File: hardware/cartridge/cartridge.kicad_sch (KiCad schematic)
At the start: 19 parts, among them U1 SN74LVC8T245PWR, U2 SN74LVC8T245PWR, U3 SN74LVC8T245PWR, U4 SN74LVC8T245PWR, U5 LCMXO2-1200HC-4TG100C, U6 MX29LV320EBTI-70G, U7 FM28V100-TG

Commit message: Fix ROM memory connections
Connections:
- net +3.3V: now also C9.1, U6.14 (WP#/ACC), U6.37 (VCC)
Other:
- moved on the sheet: C9
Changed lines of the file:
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@@
 	)
 	(junction
+		(at 129.54 60.96)
+		(diameter 0)
+		(color 0 0 0 0)
+	)
+	(junction
 		(at 351.79 227.33)
 		(diameter 0)
@@
 	(wire
 		(pts
-			(xy 107.95 60.96) (xy 125.73 60.96)
+			(xy 107.95 60.96) (xy 129.54 60.96)
 		)
 		(stroke
@@
 	(symbol
 		(lib_id "power:GND")
-		(at 133.35 60.96 90)
+		(at 137.16 60.96 90)
 		(unit 1)
 		(body_style 1)
@@
 		(fields_autoplaced yes)
 		(property "Reference" "#PWR0138"
-			(at 139.7 60.96 0)
+			(at 143.51 60.96 0)
 			(hide yes)
 			(show_name no)
@@
 		)
 		(property "Value" "GND"
-			(at 137.16 60.9599 90)
+			(at 140.97 60.9599 90)
 			(show_name no)
 			(do_not_autoplace no)
@@
 		)
 		(property "Footprint" ""
-			(at 133.35 60.96 0)
+			(at 137.16 60.96 0)
 			(hide yes)
 			(show_name no)
@@
 		)
 		(property "Datasheet" ""
-			(at 133.35 60.96 0)
+			(at 137.16 60.96 0)
 			(hide yes)
 			(show_name no)
@@
 		)
 		(property "Description" "Power symbol creates a global label with name \"GND\" , ground"
-			(at 133.35 60.96 0)
+			(at 137.16 60.96 0)
 			(hide yes)
 			(show_name no)
@@
 	)
 	(symbol
+		(lib_id "power:+3.3V")
+		(at 129.54 60.96 180)
+		(unit 1)
+		(body_style 1)
+		(exclude_from_sim no)
+		(in_bom yes)
+		(on_board yes)
+		(in_pos_files yes)
+		(dnp no)
+		(fields_autoplaced yes)
+		(property "Reference" "#PWR0292"
+			(at 129.54 57.15 0)
+			(hide yes)
+			(show_name no)
+			(do_not_autoplace no)
+			(effects
+				(font
+					(size 1.27 1.27)
+				)
+			)
+		)
+		(property "Value" "+3.3V"
+			(at 129.54 66.04 0)
+			(show_name no)
+			(do_not_autoplace no)
+			(effects
+				(font
+					(size 1.27 1.27)
+				)
+			)
+		)
+		(property "Footprint" ""
+			(at 129.54 60.96 0)
+			(hide yes)
+			(show_name no)
+			(do_not_autoplace no)
+			(effects
+				(font
+					(size 1.27 1.27)
+				)
+			)
+		)
+		(property "Datasheet" ""
+			(at 129.54 60.96 0)
+			(hide yes)
+			(show_name no)
+			(do_not_autoplace no)
+			(effects
+				(font
+					(size 1.27 1.27)
+				)
+			)
+		)
+		(property "Description" "Power symbol creates a global label with name \"+3.3V\""
+			(at 129.54 60.96 0)
+			(hide yes)
+			(show_name no)
+			(do_not_autoplace no)
+			(effects
+				(font
+					(size 1.27 1.27)
+				)
+			)
+		)
+		(pin "1"
+		)
+		(instances
+			(project "cartridge"
+				(path "/2780facd-cffd-485a-aed1-c460c817db24"
+					(reference "#PWR0292")
+					(unit 1)
+				)
+			)
+		)
+	)
+	(symbol
 		(lib_id "power:GND")
 		(at 242.57 182.88 90)
@@
 	)
 	(symbol
+		(lib_id "power:+3.3V")
+		(at 57.15 66.04 90)
+		(unit 1)
+		(body_style 1)
+		(exclude_from_sim no)
+		(in_bom yes)
+		(on_board yes)
+		(in_pos_files yes)
+		(dnp no)
+		(fields_autoplaced yes)
+		(property "Reference" "#PWR0293"
+			(at 60.96 66.04 0)
+			(hide yes)
+			(show_name no)
+			(do_not_autoplace no)
+			(effects
+				(font
+					(size 1.27 1.27)
+				)
+			)
+		)
+		(property "Value" "+3.3V"
+			(at 53.34 66.0399 90)
+			(show_name no)
+			(do_not_autoplace no)
+			(effects
+				(font
+					(size 1.27 1.27)
+				)
+				(justify left)
+			)
+		)
+		(property "Footprint" ""
+			(at 57.15 66.04 0)
+			(hide yes)
+			(show_name no)
+			(do_not_autoplace no)
+			(effects
+				(font
+					(size 1.27 1.27)
+				)
+			)
+		)
+		(property "Datasheet" ""
+			(at 57.15 66.04 0)
+			(hide yes)
+			(show_name no)
+			(do_not_autoplace no)
+			(effects
+				(font
+					(size 1.27 1.27)
+				)
+			)
+		)
+		(property "Description" "Power symbol creates a global label with name \"+3.3V\""
+			(at 57.15 66.04 0)
+			(hide yes)
+			(show_name no)
+			(do_not_autoplace no)
+			(effects
+				(font
+					(size 1.27 1.27)
+				)
+			)
+		)
+		(pin "1"
+		)
+		(instances
+			(project "cartridge"
+				(path "/2780facd-cffd-485a-aed1-c460c817db24"
+					(reference "#PWR0293")
+					(unit 1)
+				)
+			)
+		)
+	)
+	(symbol
 		(lib_id "power:VSSA")
 		(at 351.79 219.71 270)
@@
 	(symbol
 		(lib_id "Device:C")
-		(at 129.54 60.96 90)
+		(at 133.35 60.96 90)
 		(unit 1)
 		(body_style 1)
@@
 		(fields_autoplaced yes)
 		(property "Reference" "C9"
-			(at 129.54 53.34 90)
+			(at 133.35 53.34 90)
 			(show_name no)
 			(do_not_autoplace no)
@@
 		)
 		(property "Value" "100nF"
-			(at 129.54 55.88 90)
+			(at 133.35 55.88 90)
 			(show_name no)
 			(do_not_autoplace no)
@@
 		)
 		(property "Footprint" "Capacitor_SMD:C_0603_1608Metric_Pad1.08x0.95mm_HandSolder"
-			(at 133.35 59.9948 0)
+			(at 137.16 59.9948 0)
 			(hide yes)
 			(show_name no)
@@
 		)
 		(property "Datasheet" ""
-			(at 129.54 60.96 0)
+			(at 133.35 60.96 0)
 			(hide yes)
 			(show_name no)
@@
 		)
 		(property "Description" "Unpolarized capacitor"
-			(at 129.54 60.96 0)
+			(at 133.35 60.96 0)
 			(hide yes)
 			(show_name no)

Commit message: Add PCB
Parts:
- U1, U2, U3, U4: footprint PW24 -> SN74LVC8T245PWR:PW24
- U5: footprint TQFP100_LAT -> LCMXO2-1200HC-4TG100C:TQFP100_LAT
- U6: footprint TSOPI48L12X20NORMAL_MAC -> MX29LV320EBTI-70G:TSOPI48L12X20NORMAL_MAC
- U7: footprint TSOP-32 -> FM28V100-TG:TSOP-32
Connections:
- net gb_a1: now also U1.3 (A1)
- net gb_a10: no longer U1.5 (A3)
- net gb_a11: no longer U1.6 (A4)
- net gb_a12: no longer U1.7 (A5)
- net gb_a13: no longer U1.8 (A6)
- net gb_a14: no longer U1.9 (A7)
- net gb_a15: no longer U1.10 (A8)
- net gb_a2: now also U1.4 (A2)
- net gb_a3: now also U1.5 (A3)
- net gb_a4: now also U1.6 (A4)
- net gb_a5: now also U1.7 (A5)
- net gb_a6: now also U1.8 (A6)
- net gb_a7: now also U1.9 (A7)
- net gb_a8: now also U1.10 (A8); no longer U1.3 (A1)
- net gb_a9: no longer U1.4 (A2)
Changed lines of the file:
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@@
 			)
 		)
-		(property "Footprint" "PW24"
+		(property "Footprint" "SN74LVC8T245PWR:PW24"
 			(at 182.88 207.01 0)
 			(hide yes)
@@
 			)
 		)
-		(property "Footprint" "TQFP100_LAT"
+		(property "Footprint" "LCMXO2-1200HC-4TG100C:TQFP100_LAT"
 			(at 57.15 121.92 0)
 			(hide yes)
@@
 		(in_pos_files yes)
 		(dnp no)
-		(fields_autoplaced yes)
 		(property "Reference" "#PWR046"
 			(at 185.42 160.02 0)
@@
 			)
 		)
-		(property "Value" "gb_a8"
-			(at 177.8 160.0199 90)
+		(property "Value" "gb_a1"
+			(at 175.006 160.02 90)
 			(show_name no)
 			(do_not_autoplace no)
@@
 					(size 1.27 1.27)
 				)
-				(justify left)
 			)
 		)
@@
 		(in_pos_files yes)
 		(dnp no)
-		(fields_autoplaced yes)
 		(property "Reference" "#PWR067"
 			(at 185.42 165.1 0)
@@
 			)
 		)
-		(property "Value" "gb_a10"
-			(at 177.8 165.0999 90)
+		(property "Value" "gb_a3"
+			(at 174.752 165.1 90)
 			(show_name no)
 			(do_not_autoplace no)
@@
 					(size 1.27 1.27)
 				)
-				(justify left)
 			)
 		)
@@
 		(in_pos_files yes)
 		(dnp no)
-		(fields_autoplaced yes)
 		(property "Reference" "#PWR0209"
 			(at 185.42 177.8 0)
@@
 			)
 		)
-		(property "Value" "gb_a15"
-			(at 177.8 177.7999 90)
+		(property "Value" "gb_a8"
+			(at 174.752 177.546 90)
 			(show_name no)
 			(do_not_autoplace no)
@@
 					(size 1.27 1.27)
 				)
-				(justify left)
 			)
 		)
@@
 		(in_pos_files yes)
 		(dnp no)
-		(fields_autoplaced yes)
 		(property "Reference" "#PWR0208"
 			(at 185.42 175.26 0)
@@
 			)
 		)
-		(property "Value" "gb_a14"
-			(at 177.8 175.2599 90)
+		(property "Value" "gb_a7"
+			(at 174.752 175.26 90)
 			(show_name no)
 			(do_not_autoplace no)
@@
 					(size 1.27 1.27)
 				)
-				(justify left)
 			)
 		)
@@
 		(in_pos_files yes)
 		(dnp no)
-		(fields_autoplaced yes)
 		(property "Reference" "#PWR049"
 			(at 185.42 162.56 0)
@@
 			)
 		)
-		(property "Value" "gb_a9"
-			(at 177.8 162.5599 90)
+		(property "Value" "gb_a2"
+			(at 174.752 162.56 90)
 			(show_name no)
 			(do_not_autoplace no)
@@
 					(size 1.27 1.27)
 				)
-				(justify left)
 			)
 		)
@@
 			)
 		)
-		(property "Footprint" "PW24"
+		(property "Footprint" "SN74LVC8T245PWR:PW24"
 			(at 181.61 154.94 0)
 			(hide yes)
@@
 		(in_pos_files yes)
 		(dnp no)
-		(fields_autoplaced yes)
 		(property "Reference" "#PWR0206"
 			(at 185.42 170.18 0)
@@
 			)
 		)
-		(property "Value" "gb_a12"
-			(at 177.8 170.1799 90)
+		(property "Value" "gb_a5"
+			(at 174.752 170.18 90)
 			(show_name no)
 			(do_not_autoplace no)
@@
 					(size 1.27 1.27)
 				)
-				(justify left)
 			)
 		)
@@
 		(in_pos_files yes)
 		(dnp no)
-		(fields_autoplaced yes)
 		(property "Reference" "#PWR088"
 			(at 185.42 167.64 0)
@@
 			)
 		)
-		(property "Value" "gb_a11"
-			(at 177.8 167.6399 90)
+		(property "Value" "gb_a4"
+			(at 174.752 167.64 90)
 			(show_name no)
 			(do_not_autoplace no)
@@
 					(size 1.27 1.27)
 				)
-				(justify left)
 			)
 		)
@@
 			)
 		)
-		(property "Footprint" "TSOPI48L12X20NORMAL_MAC"
+		(property "Footprint" "MX29LV320EBTI-70G:TSOPI48L12X20NORMAL_MAC"
 			(at 57.15 33.02 0)
 			(hide yes)
@@
 			)
 		)
-		(property "Footprint" "PW24"
+		(property "Footprint" "SN74LVC8T245PWR:PW24"
 			(at 290.83 207.01 0)
 			(hide yes)
@@
 			)
 		)
-		(property "Footprint" "TSOP-32"
+		(property "Footprint" "FM28V100-TG:TSOP-32"
 			(at 185.42 31.75 0)
 			(hide yes)
@@
 		(in_pos_files yes)
 		(dnp no)
-		(fields_autoplaced yes)
 		(property "Reference" "#PWR0207"
 			(at 185.42 172.72 0)
@@
 			)
 		)
-		(property "Value" "gb_a13"
-			(at 177.8 172.7199 90)
+		(property "Value" "gb_a6"
+			(at 174.752 172.72 90)
 			(show_name no)
 			(do_not_autoplace no)
@@
 					(size 1.27 1.27)
 				)
-				(justify left)
 			)
 		)
@@
 			)
 		)
-		(property "Footprint" "PW24"
+		(property "Footprint" "SN74LVC8T245PWR:PW24"
 			(at 290.83 154.94 0)
 			(hide yes)

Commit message: Add RP2040, caps, 3D models
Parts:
- added C11, C12, C13, C14, C15, C16, C17, C18, C19, C20: 100nF, Capacitor_SMD:C_0603_1608Metric_Pad1.08x0.95mm_HandSolder, symbol Device:C
- added R4: 10K, Resistor_SMD:R_0603_1608Metric_Pad0.98x0.95mm_HandSolder, symbol Device:R
- added U8: RP2040-Zero, RP2040-Zero:RP2040-Zero, symbol RP2040-Zero:RP2040-Zero
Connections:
- net +3.3V: now also C11.1, C12.1, C13.1, C14.1, C15.1, C16.1, C17.1, C18.1, C19.1, C20.1, U8.3v3
- net GND: now also C11.2, C12.2, C13.2, C14.2, C15.2, C16.2, C17.2, C18.2, C19.2, C20.2, R4.1, U8.GND
- net data_dir: now also R4.2
- new net +5V (USB): U8.5v

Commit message: Add spi_bringup (draft)
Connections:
- net SPI_MOSI: now reaches U5.96 (PT10B)
- net SPI_MOSI: now also U8.3
- net SPI_CS_N: now reaches U5.97 (PT10A)
- net SPI_CS_N: now also U8.1
- net SPI_SCK: now reaches U5.98 (PT9B)
- net SPI_SCK: now also U8.2
- net SPI_MISO: now reaches U5.99 (PT9A)
- net SPI_MISO: now also U8.0
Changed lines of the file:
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@@
 		)
+	)
+	(label "SPI_MISO"
+		(at 304.8 30.48 0)
+		(effects (font (size 1.27 1.27)) (justify left bottom))
+	)
+	(label "SPI_CS_N"
+		(at 304.8 33.02 0)
+		(effects (font (size 1.27 1.27)) (justify left bottom))
+	)
+	(label "SPI_SCK"
+		(at 304.8 35.56 0)
+		(effects (font (size 1.27 1.27)) (justify left bottom))
+	)
+	(label "SPI_MOSI"
+		(at 304.8 38.1 0)
+		(effects (font (size 1.27 1.27)) (justify left bottom))
+	)
+	(label "SPI_MISO"
+		(at 128.27 124.46 0)
+		(effects (font (size 1.27 1.27)) (justify left bottom))
+	)
+	(label "SPI_CS_N"
+		(at 128.27 129.54 0)
+		(effects (font (size 1.27 1.27)) (justify left bottom))
+	)
+	(label "SPI_SCK"
+		(at 128.27 127 0)
+		(effects (font (size 1.27 1.27)) (justify left bottom))
+	)
+	(label "SPI_MOSI"
+		(at 128.27 132.08 0)
+		(effects (font (size 1.27 1.27)) (justify left bottom))
 	)
 	(sheet_instances

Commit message: Update schematics
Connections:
- net +3.3V: no longer U5.58 (PR9A)
- net data_oe_n: now reaches R3.1, U3.22 (*OE)
- net data_oe_n: now also U5.58 (PR9A)
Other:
- moved on the sheet: C12

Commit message: Update schematics
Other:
- moved on the sheet: C12

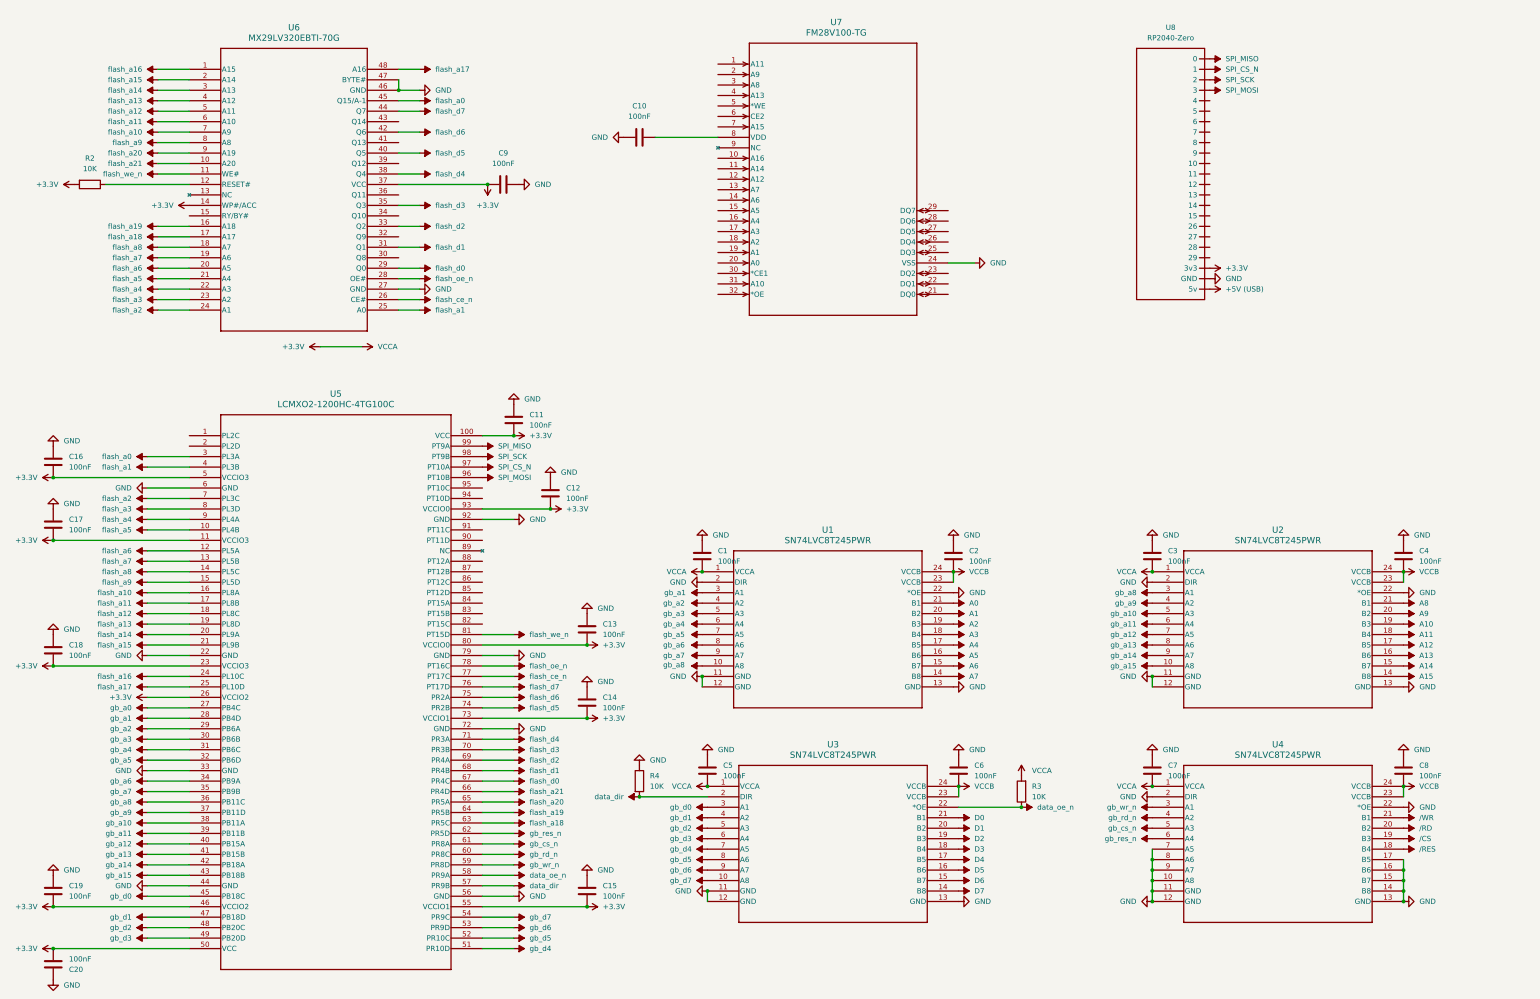
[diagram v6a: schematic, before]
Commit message: Update plan and schematics
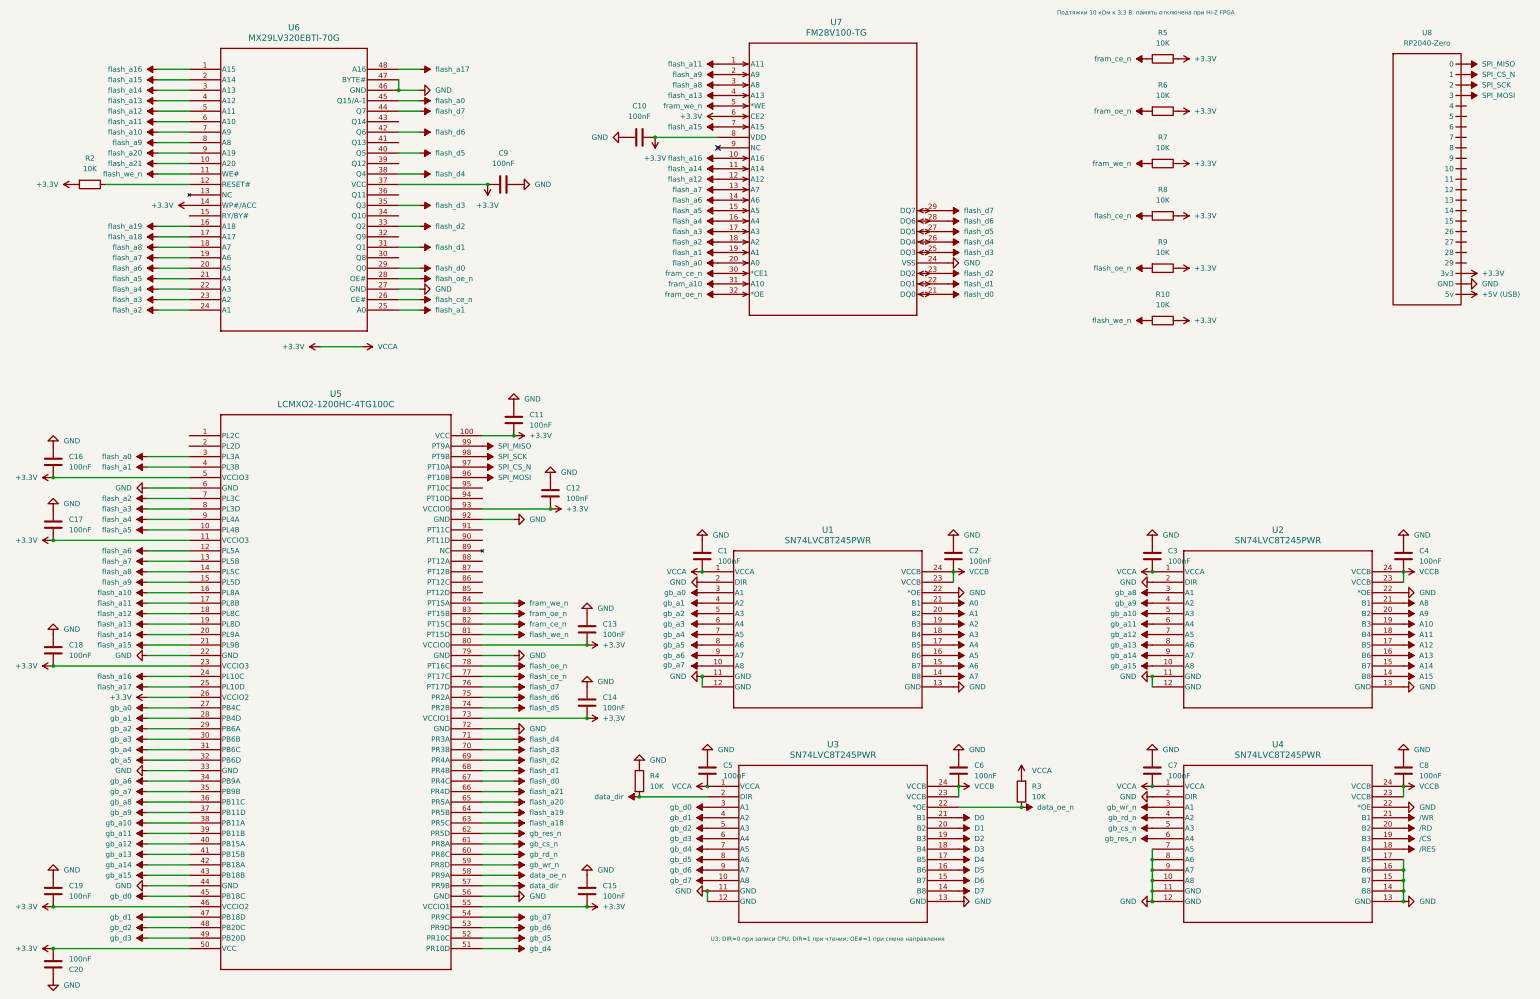
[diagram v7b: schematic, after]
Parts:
- added R10, R5, R6, R7, R8, R9: 10K, Resistor_SMD:R_0603_1608Metric_Pad0.98x0.95mm_HandSolder, symbol Device:R
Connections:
- net +3.3V: now also C10.1, U7.6 (CE2), U7.8 (VDD), R10.1, R5.1, R6.1, R7.1, R8.1, R9.1
- net flash_a0: now also U7.20 (A0)
- net flash_a1: now also U7.19 (A1)
- net flash_a11: now also U7.1 (A11)
- net flash_a12: now also U7.12 (A12)
- net flash_a13: now also U7.4 (A13)
- net flash_a14: now also U7.11 (A14)
- net flash_a15: now also U7.7 (A15)
- net flash_a16: now also U7.10 (A16)
- net flash_a2: now also U7.18 (A2)
- net flash_a3: now also U7.17 (A3)
- net flash_a4: now also U7.16 (A4)
- net flash_a5: now also U7.15 (A5)
- net flash_a6: now also U7.14 (A6)
- net flash_a7: now also U7.13 (A7)
- net flash_a8: now also U7.3 (A8)
- net flash_a9: now also U7.2 (A9)
- net flash_ce_n: now also R8.2
- net flash_d0: now also U7.21 (DQ0)
- net flash_d1: now also U7.22 (DQ1)
- net flash_d2: now also U7.23 (DQ2)
- net flash_d3: now also U7.25 (DQ3)
- net flash_d4: now also U7.26 (DQ4)
- net flash_d5: now also U7.27 (DQ5)
- net flash_d6: now also U7.28 (DQ6)
- net flash_d7: now also U7.29 (DQ7)
- net flash_oe_n: now also R9.2
- net flash_we_n: now also R10.2
- net gb_a0: now also U1.3 (A1)
- net gb_a1: now also U1.4 (A2); no longer U1.3 (A1)
- net gb_a2: now also U1.5 (A3); no longer U1.4 (A2)
- net gb_a3: now also U1.6 (A4); no longer U1.5 (A3)
- net gb_a4: now also U1.7 (A5); no longer U1.6 (A4)
- net gb_a5: now also U1.8 (A6); no longer U1.7 (A5)
- net gb_a6: now also U1.9 (A7); no longer U1.8 (A6)
- net gb_a7: now also U1.10 (A8); no longer U1.9 (A7)
- net gb_a8: no longer U1.10 (A8)
- net fram_ce_n: now reaches U5.82 (PT15C)
- net fram_ce_n: now also U7.30 (*CE1), R5.2
- net fram_oe_n: now reaches U5.83 (PT15B)
- net fram_oe_n: now also U7.32 (*OE), R6.2
- net fram_we_n: now reaches U5.84 (PT15A)
- net fram_we_n: now also U7.5 (*WE), R7.2
- net fram_a10: now reaches U7.31 (A10)
- no-connect marks 0 -> 1
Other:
- note added: "U3: DIR=0 при записи CPU, DIR=1 при чтении; OE#=1 при смене направления"
- note added: "Подтяжки 10 кОм к 3,3 В: память отключена при Hi-Z FPGA"
- moved on the sheet: U8

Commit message: add game_mbc5 target
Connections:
- net fram_a10 is gone; now on net flash_a10: U7.31 (A10)
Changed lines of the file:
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@@
 			)
 		)
-		(property "Value" "fram_a10"
+		(property "Value" "flash_a10"
 			(at 181.61 85.0899 90)
 			(show_name no)
